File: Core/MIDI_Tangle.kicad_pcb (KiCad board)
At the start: 2 copper layers, 40 x 97.5 mm, 97 parts, among them J1 USB_C_Receptacle_USB2.0, J2 Conn_01x04, J21 Conn_02x08_Odd_Even, J4 Conn_01x06_Male, J5 Conn_01x08_Female, J6 Conn_01x08_Female, J7 Conn_01x08_Female, J8 Conn_01x08_Female, Q1 BSS84, Q2 2N7002, Q3 BSS84, SW1 SW_Push_DPDT, SW2 SW_SPST, SW3 SW_SPST, U1 ATSAMD21G15B-A, U10 TL072, U11 TL072, U12 TL072, U13 TL072, U14 MCP2517FD-xSL, U15 MCP2562FD-ESN, U16 CAT250xxx, U17 74HC595, U18 MIC5504-3.3YM5, U19 74HC595, U2 DG408, U20 74HC595, U3 DG408, U4 DG408, U5 DG408, U6 DG408, U7 DG408, U8 DG408, U9 DG408, Y1 20MHz

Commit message: Finalize module
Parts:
- R11, R12: footprint Resistor_SMD:R_0603_1608Metric -> Resistor_SMD:R_0805_2012Metric
- moved R12 2.61 mm to (175.2, 55.8)
- moved C41 0.36 mm to (176.2, 57.5)
- moved R11 0.24 mm to (172.8, 57.8)
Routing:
- net Net-(R12-Pad2): track 1.71 -> 2.65 mm
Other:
- rule pad_to_mask_clearance: 0.05 -> 0

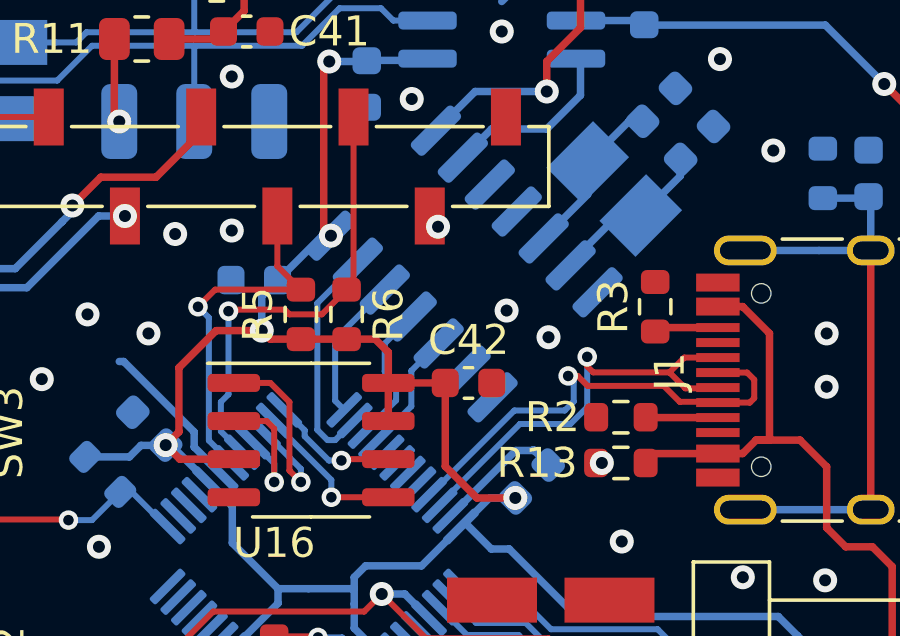
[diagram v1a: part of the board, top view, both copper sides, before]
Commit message: Connect CAN_INT
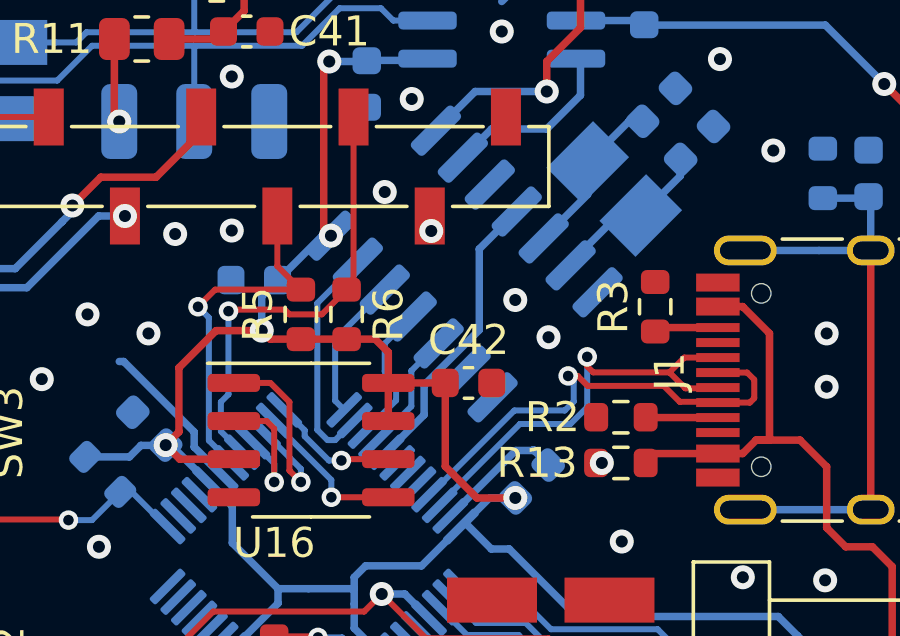
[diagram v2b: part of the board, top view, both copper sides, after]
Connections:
- U1 pad 29: unconnected-(U1-PA20-Pad29) -> CAN_INT
- U14 pad 4: unconnected-(U14-~{INT}-Pad4) -> CAN_INT
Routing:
- net CAN_INT: track 0.00 -> 9.82 mm
- net GND: vias 116 -> 117
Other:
- board text added: "M2IDI_Tangle V1.2 GuavTek"
- board text removed: "M2IDI_Tangle V1.1 GuavTek"
